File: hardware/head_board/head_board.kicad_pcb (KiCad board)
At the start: 4 copper layers, 80 x 64.4 mm, 138 parts, among them J2 8P8C, J3 CAM, J4 CAMLED, J5 AUX, J7 MOTOR, J8 MOTOR, J9 MOTOR, SW1 BOOTSEL, U1 VX7805-500, U10 TMC2209, U2 MIC5317-3.3, U3 RP2040, U4 W25Q128JVS, U5 TVS, U6 TVS, U7 74HC2G34, U8 TMC2209, U9 TMC2209, Y1 12MHz

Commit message: V2 of the head board (Jellyfish)
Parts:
- added ?: , Graphics, F.Cu at (116.5, 103.1)
- added ?: , Graphics, B.Cu at (105.4, 60.3)
- added ?: , Graphics, B.Cu at (113.4, 63.2)
- added ?: , Graphics, B.Cu at (105.3, 85.4)
- added ?: , Graphics, B.Cu at (105.8, 93.2)
- added ?: , Graphics, F.Cu at (105.2, 93.2)
- added ?: , Graphics, F.Cu at (85.8, 103.1)
- added ?: , Graphics, F.Cu at (141.2, 101.0)
- added ?: , Graphics, F.Cu at (126.0, 103.1)
- added ?: , Graphics, F.Cu at (92.8, 103.1)
- added ?: , Graphics, F.Cu at (100.8, 103.1)
- added ?: , Graphics, F.Cu at (107.5, 103.1)
- added ?: , Graphics, B.Cu at (96.8, 63.2)
- added C1: 100n, Capacitor_SMD:C_0402_1005Metric_Pad0.74x0.62mm_HandSolder, F.Cu at (111.8, 99.8)
- added D1: AUX, winterbloom:LED_0805_Kingbright_APT2012, F.Cu at (141.0, 89.5)
- added J1: INS, Connector_JST:JST_SH_BM04B-SRSS-TB_1x04-1MP_P1.00mm_Vertical, F.Cu at (107.5, 107.5)
- added J10: Stemma QT, Connector_JST:JST_SH_BM04B-SRSS-TB_1x04-1MP_P1.00mm_Vertical, F.Cu at (125.5, 107.5)
- added J6: BLTOUCH, Connector_JST:JST_SH_BM05B-SRSS-TB_1x05-1MP_P1.00mm_Vertical, F.Cu at (116.5, 107.5)
- added R1: 5.1k, Resistor_SMD:R_0402_1005Metric_Pad0.72x0.64mm_HandSolder, F.Cu at (84.7, 100.4)
- added R15: 5.1k, Resistor_SMD:R_0402_1005Metric_Pad0.72x0.64mm_HandSolder, F.Cu at (113.5, 99.8)
- added R16: 100, Resistor_SMD:R_0402_1005Metric_Pad0.72x0.64mm_HandSolder, F.Cu at (104.5, 99.8)
- added R2: 5.1k, Resistor_SMD:R_0402_1005Metric_Pad0.72x0.64mm_HandSolder, F.Cu at (84.7, 89.4)
- added R26: 5.1k, Resistor_SMD:R_0402_1005Metric_Pad0.72x0.64mm_HandSolder, F.Cu at (136.2, 100.0)
- added R27: 5.1k, Resistor_SMD:R_0402_1005Metric_Pad0.72x0.64mm_HandSolder, F.Cu at (134.8, 100.0)
- added R28: 1k, Resistor_SMD:R_0603_1608Metric_Pad0.98x0.95mm_HandSolder, F.Cu at (141.0, 85.0)
- added R3: 100, Resistor_SMD:R_0402_1005Metric_Pad0.72x0.64mm_HandSolder, F.Cu at (106.2, 99.8)
- J2: value 8P8C -> 8P8C_LED_Shielded; footprint winterbloom:Connector_RJ45_ASSMANN_A-2014-2S-4-N-R -> winterbloom:RJ45_Amphenol_RJE45-188-1411_Vertical
- J3: footprint Connector_JST:JST_XH_B4B-XH-AM_1x04_P2.50mm_Vertical -> Connector_JST:JST_SH_BM04B-SRSS-TB_1x04-1MP_P1.00mm_Vertical
- J4: footprint Connector_JST:JST_XH_B3B-XH-AM_1x03_P2.50mm_Vertical -> Connector_JST:JST_SH_BM03B-SRSS-TB_1x03-1MP_P1.00mm_Vertical
- J5: value AUX -> OUT1; footprint Connector_JST:JST_XH_B3B-XH-AM_1x03_P2.50mm_Vertical -> Connector_JST:JST_SH_BM03B-SRSS-TB_1x03-1MP_P1.00mm_Vertical
- U5: value TVS -> 74HC2G34; footprint Package_TO_SOT_SMD:SOT-23-6 -> Package_TO_SOT_SMD:SOT-363_SC-70-6
- moved U5 23.8 mm to (109.0, 99.4)
- moved R14 22.8 mm to (95.8, 99.8)
- moved C27 19.7 mm to (97.2, 99.8), turned to 90 degrees
- moved J5 19.2 mm to (99.5, 107.5)
- moved C5 17.2 mm to (105.2, 78.0), turned to -90 degrees
- moved U7 16.3 mm to (100.0, 99.4), turned to 180 degrees
- moved J4 15.6 mm to (92.0, 107.5)
- moved J3 12.6 mm to (84.0, 107.5)
- moved R13 11.0 mm to (102.8, 99.8)
- moved R9 10.8 mm to (125.8, 100.0), turned to 90 degrees
- moved C2 9.71 mm to (85.8, 83.8)
- moved TP2 9.12 mm to (78.3, 83.0)
- moved C4 8.77 mm to (101.5, 85.0)
- moved U1 8.75 mm to (91.4, 86.0)
- moved U6 8.61 mm to (94.0, 91.0)
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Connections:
- net Net-(C2-Pad1) renamed /Power/VIN_FILTERED
- net Net-(C28-Pad1) renamed /Left Motor/CPO
- net Net-(C28-Pad2) renamed /Left Motor/CPI
- net Net-(C30-Pad2) renamed /Left Motor/VCP
- net Net-(C31-Pad1) renamed /Left Motor/5VOUT
- net Net-(C32-Pad1) renamed /Left Motor/BRB
- net Net-(C33-Pad1) renamed /Left Motor/BRA
- net Net-(C42-Pad1) renamed /Z Motor/CPO
- net Net-(C42-Pad2) renamed /Z Motor/CPI
- net Net-(C44-Pad2) renamed /Z Motor/VCP
- net Net-(C45-Pad1) renamed /Z Motor/5VOUT
- net Net-(C46-Pad1) renamed /Z Motor/BRB
- net Net-(C47-Pad1) renamed /Z Motor/BRA
- net Net-(C56-Pad1) renamed /Right Motor/CPO
- net Net-(C56-Pad2) renamed /Right Motor/CPI
- net Net-(C58-Pad2) renamed /Right Motor/VCP
- net Net-(C59-Pad1) renamed /Right Motor/5VOUT
- net Net-(C60-Pad1) renamed /Right Motor/BRB
- net Net-(C61-Pad1) renamed /Right Motor/BRA
- J2 pad 1: +24V -> /Connections/CAM_D+
- J2 pad 2: +24V -> /Connections/CAM_D-
- J2 pad 4: GND -> /Microcontroller/USB_D+
- J2 pad 5: /Connections/CAM_D- -> /Microcontroller/USB_D-
- J2 pad 6: /Connections/CAM_D+ -> +24V
- J2 pad 7: /Microcontroller/USB_D- -> GND
- J2 pad 8: /Microcontroller/USB_D+ -> +24V
- U3 pad 13: unconnected-(U3-Pad13) -> /Connections/QWIIC_SDA
- U3 pad 14: unconnected-(U3-Pad14) -> /Connections/QWIIC_SCL
- U3 pad 16: unconnected-(U3-Pad16) -> /Microcontroller/AUX_LED
- U3 pad 4: unconnected-(U3-Pad4) -> /Connections/IN_1
- U3 pad 5: unconnected-(U3-Pad5) -> /Connections/IN_2
- U3 pad 6: unconnected-(U3-Pad6) -> /Connections/BLTOUCH_CONTROL
- U3 pad 7: unconnected-(U3-Pad7) -> /Connections/BLTOUCH_OUT
- U5 pad 1: /Connections/CAM_D- -> Net-(R3-Pad1)
- U5 pad 3: /Connections/CAM_D+ -> Net-(R16-Pad1)
- U5 pad 4: /Connections/CAM_D+ -> /Connections/IN_2
- U5 pad 5: +5V -> +3V3
- U5 pad 6: /Connections/CAM_D- -> /Connections/IN_1
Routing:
- net VMOTOR: track 137.4 -> 22.0 mm, vias 10 -> 12
- net GND: track 168.6 -> 56.0 mm, vias 84 -> 140
- net /Connections/AUX_OUT: track 19.4 -> 48.6 mm
- net /Connections/BLTOUCH_OUT: track 0.00 -> 28.3 mm, vias 0 -> 2
- net /Connections/IN_2: track 0.00 -> 24.8 mm, vias 0 -> 2
- net /Connections/QWIIC_SCL: track 0.00 -> 23.7 mm, vias 0 -> 3
- net /Connections/IN_1: track 0.00 -> 23.2 mm, vias 0 -> 2
- net /Connections/QWIIC_SDA: track 0.00 -> 23.2 mm, vias 0 -> 3
- net /Power/VIN_FILTERED: track 22.6 -> 0.00 mm
- net /Connections/BLTOUCH_CONTROL: track 0.00 -> 21.0 mm, vias 0 -> 2
- net +3V3: track 183.7 -> 163.2 mm, vias 15 -> 20
- net /Microcontroller/USB_D-: track 70.7 -> 56.4 mm
- net /Microcontroller/M2_EN: track 56.4 -> 69.6 mm
- net /Microcontroller/QSPI_CS: track 22.0 -> 9.52 mm, vias 2 -> 0
- net /Microcontroller/AUX_LED: track 0.00 -> 12.2 mm, vias 0 -> 2
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- added copper zone on In2.Cu, net +24V
- added copper zone on F.Cu, net /Power/VIN_FILTERED
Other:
- board size 80 x 64.4 mm -> 80 x 70 mm
- board text added: "${COMMENT1} ${COMMENT2}"
- board text added: "${COMPANY} ${COMMENT3} ${REVISION} ${ISSUE_DATE}"
- board text added: "PCB Specifications: - 4 copper layers - Size: 80 x 70 mm - Thickness: 1.6 mm - Material: FR4 TG-140+ - Min track width/spacing: 0.153 mm (5 mil) - Min hole size: 0.3 mm - Soldermask: Pink/Purple/Matte Black - Silkscreen: Black/White - Finish: ENIG 2U{dblquote} - Copper: 1 oz - UL Marking: on top silkscreen"
- board text removed: "${TITLE} ${REVISION} ${ISSUE_DATE} ${COMPANY} ${COMMENT3} ${COMMENT2} ${COMMENT1}"
- board text removed: "AUX"
- board text removed: "CAMERA"
- board text removed: "LED"
- board text removed: "PCB Specifications: - 2 copper layers - Size: 100 x 30 mm - Thickness: 1.6 mm - Material: FR4 TG-140+ - Min track width/spacing: 0.153 mm (5 mil) - Min hole size: 0.3 mm - Soldermask: Pink/Purple/Matte Black - Silkscreen: Black/White - Finish: ENIG 2U{dblquote} - Copper: 1 oz - UL Marking: on bottom silkscreen"

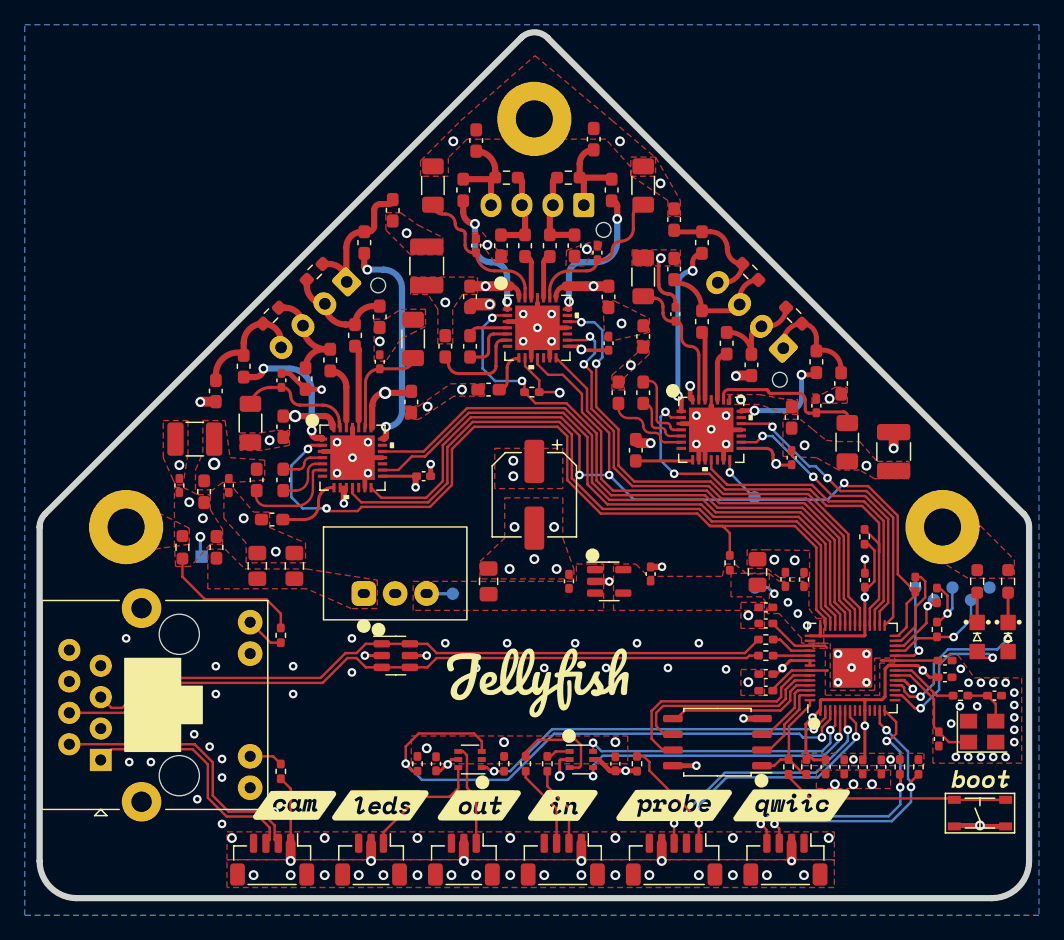
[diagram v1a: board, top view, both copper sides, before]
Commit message: Replace veritcal connectors with horizontal ones
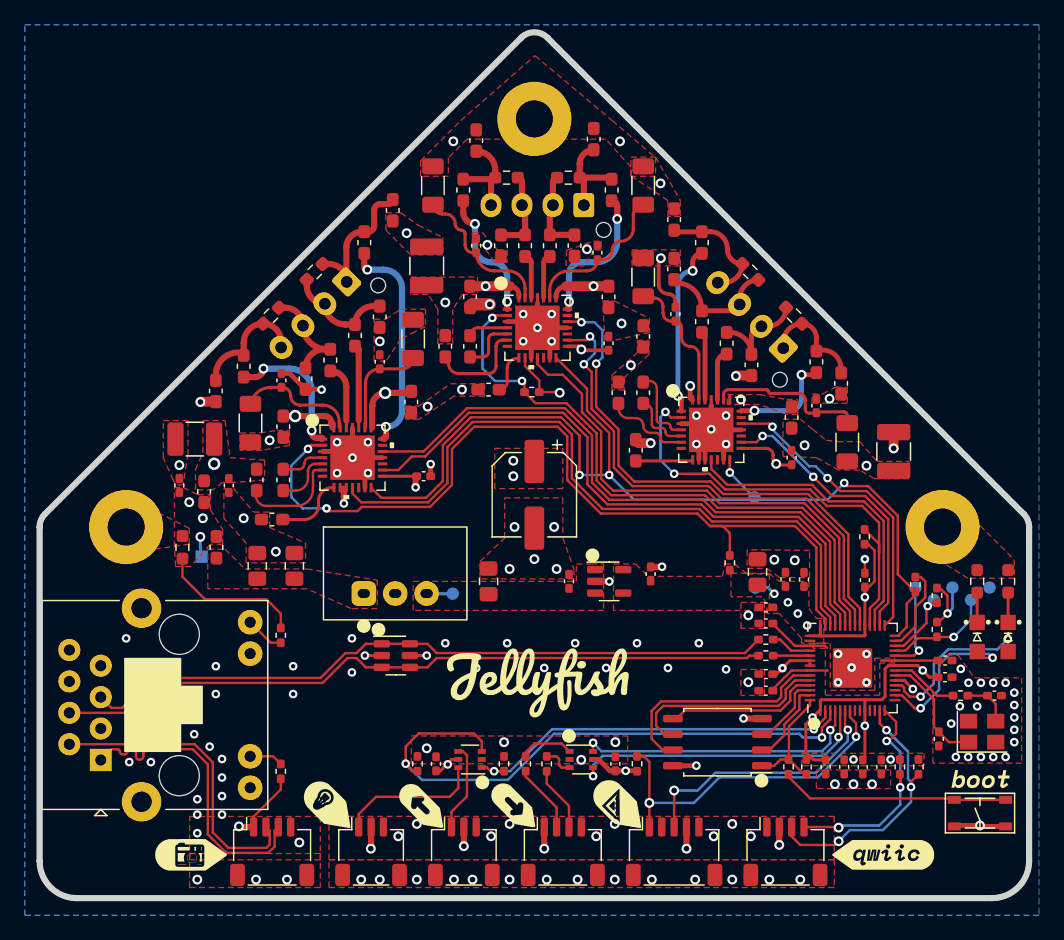
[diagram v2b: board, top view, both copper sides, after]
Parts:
- removed the ? at (116.5, 103.1)
- removed the ? at (85.8, 103.1)
- removed the ? at (126.0, 103.1)
- removed the ? at (92.8, 103.1)
- removed the ? at (100.8, 103.1)
- removed the ? at (107.5, 103.1)
- added ?: , Graphics, F.Cu at (133.6, 107.1)
- added ?: , Graphics, F.Cu at (111.9, 103.0)
- added ?: , Graphics, F.Cu at (103.5, 103.1)
- added ?: , Graphics, F.Cu at (77.2, 107.1)
- added ?: , Graphics, F.Cu at (88.5, 103.1)
- added ?: , Graphics, F.Cu at (96.0, 103.2)
- J1, J10, J3: footprint Connector_JST:JST_SH_BM04B-SRSS-TB_1x04-1MP_P1.00mm_Vertical -> Connector_JST:JST_SH_SM04B-SRSS-TB_1x04-1MP_P1.00mm_Horizontal
- J4, J5: footprint Connector_JST:JST_SH_BM03B-SRSS-TB_1x03-1MP_P1.00mm_Vertical -> Connector_JST:JST_SH_SM03B-SRSS-TB_1x03-1MP_P1.00mm_Horizontal
- J6: footprint Connector_JST:JST_SH_BM05B-SRSS-TB_1x05-1MP_P1.00mm_Vertical -> Connector_JST:JST_SH_SM05B-SRSS-TB_1x05-1MP_P1.00mm_Horizontal
- moved R3 1.75 mm to (104.5, 99.8)
- moved R16 1.70 mm to (106.2, 99.8)
- moved J1 0.64 mm to (107.5, 106.9), turned to 0 degrees
- moved J10 0.64 mm to (125.5, 106.9), turned to 0 degrees
- moved J3 0.64 mm to (84.0, 106.9), turned to 0 degrees
- moved J4 0.64 mm to (92.0, 106.9), turned to 0 degrees
- moved J5 0.64 mm to (99.5, 106.9), turned to 0 degrees
- moved J6 0.64 mm to (116.5, 106.9), turned to 0 degrees
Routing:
- net +5V: track 71.2 -> 80.5 mm
- net Net-(R16-Pad1): track 8.07 -> 2.52 mm
- net /Connections/QWIIC_SCL: track 23.7 -> 18.6 mm
- net /Connections/CAM_D+: track 19.6 -> 24.7 mm
- net Net-(R3-Pad1): track 1.97 -> 4.45 mm
- net /Connections/CAM_D-: track 22.5 -> 24.6 mm
- net GND: track 56.0 -> 54.1 mm, vias 140 -> 146
- net Net-(R16-Pad2): track 6.86 -> 5.26 mm
- net Net-(J4-Pad1): track 10.1 -> 11.6 mm
- net /Connections/QWIIC_SDA: track 23.2 -> 21.9 mm
- net Net-(J5-Pad1): track 8.24 -> 7.13 mm
- net Net-(R3-Pad2): track 6.55 -> 5.55 mm
- net +3V3: track 163.2 -> 162.3 mm
- net /Connections/BLTOUCH_OUT: track 28.3 -> 27.8 mm
